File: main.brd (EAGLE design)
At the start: 50.8 x 50.8 mm, 93 parts, among them Q1 5.8A/30V/35mΩ, Q2 5.8A/30V/35mΩ, Q3 2.5A/30V/105mΩ, U1 BQ24133_RGY_24, U2 SN65HVD32_D_8

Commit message: Some layout stuff, package changes
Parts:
- removed 3.3-PWR, ACT, LED: 2V @ 20mA, adafruit:CHIPLED_0603
- removed JP1: (no value), pinhead:1X05
- removed R29, R30: 65, resistor:R0603
- added GPIO: (no value), pinhead:1X10
- added LED0, LED1: 2V @ 20mA, adafruit:CHIPLED_0603
- added R28: 64.9, resistor:R0603
- C10, C11, C12, C14, C15, C18, C19, C20, C21, C25: device rcl:C1206 -> resistor:C0603
- R14, R15, R16, R17, R18: value 1.32k -> ?
- R19, R20, R21, R24, R25: value 680 -> ?
- R41, R42: value 65 -> 64.9
- moved GND-JMP 127.8 mm to (46.5, -28.4)
- moved C23 79.0 mm to (43.1, 16.9), turned to 0 degrees
- moved SD 78.1 mm to (40.8, 26.6), turned to 270 degrees
- moved R31 75.6 mm to (37.0, 17.3), turned to 180 degrees
- moved C9 50.4 mm to (37.8, 35.8)
- moved C1 49.1 mm to (25.1, 33.0), turned to 0 degrees
- moved R27 47.0 mm to (-2.62, -16.5), turned to 270 degrees
- moved AIN 46.1 mm to (2.44, 31.9), turned to 90 degrees
- moved C2 46.1 mm to (25.1, 35.2), turned to 0 degrees
- moved R8 45.9 mm to (-1.91, -21.7), turned to 270 degrees
- moved S2 45.8 mm to (56.9, -17.7), turned to 90 degrees
- moved BATT 45.2 mm to (-0.89, -12.0), turned to 90 degrees
- moved R5 45.2 mm to (23.9, 40.0)
- moved L2 44.7 mm to (-1.55, -19.1), turned to 180 degrees
- moved L6 43.1 mm to (17.3, 43.7), turned to 0 degrees
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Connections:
- removed net LED: MCU.28, R41.1
- removed net N$29: LED.A, R41.2
- removed net VOS: C6.1, L1.2, R3.2, TPS62162-Q1.6
- new net GPIO10: GPIO.10
- new net GPIO6: GPIO.6
- new net GPIO7: GPIO.7
- new net GPIO8: GPIO.8
- new net GPIO9: GPIO.9
- new net N$7: LED0.C, R41.2
- net 3.3V: now also C6.1, L1.2, LED0.A, LED1.A, R3.2, TPS62162-Q1.6; no longer R29.1
- net GND: no longer 3.3-PWR.C, LED.C
- net GPIO1: now also GPIO.1; no longer JP1.1
- net GPIO2: now also GPIO.2; no longer JP1.2
- net GPIO3: now also GPIO.3; no longer JP1.3
- net GPIO4: now also GPIO.4; no longer JP1.4
- net GPIO5: now also GPIO.5; no longer JP1.5
- net N$19: now also SD.2; no longer 3.3-PWR.A, R29.2
- net N$20: now also LED1.C, R28.2; no longer ACT.A, R30.1
- net PB09D_SER4_P1: no longer R30.2
- net SD_CS: no longer ACT.C, SD.2
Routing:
- net AGND: track 37.1 -> 40.2 mm
- net BATT: track 28.2 -> 30.6 mm
- net PC_ACN: track 11.7 -> 12.4 mm
- net PC_VREF: track 16.8 -> 16.2 mm
- net PC_TTC: track 5.02 -> 5.57 mm
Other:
- outline, holes or cut-outs redrawn

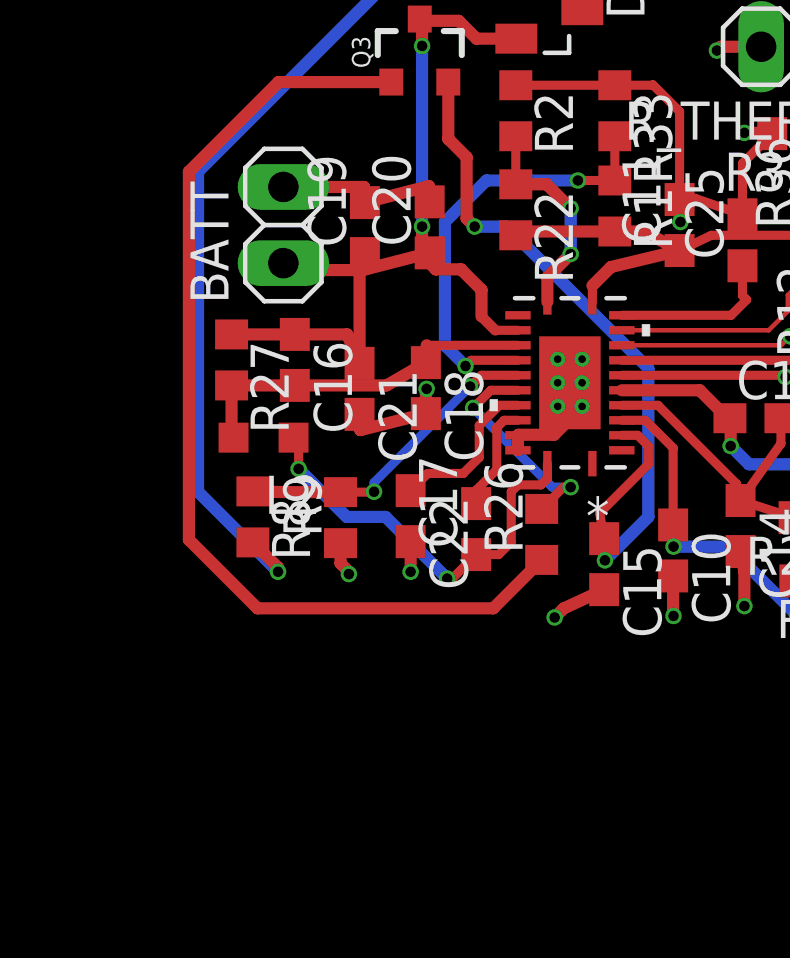
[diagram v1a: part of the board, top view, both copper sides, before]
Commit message: Seperated grounds, added pullup to cell pin
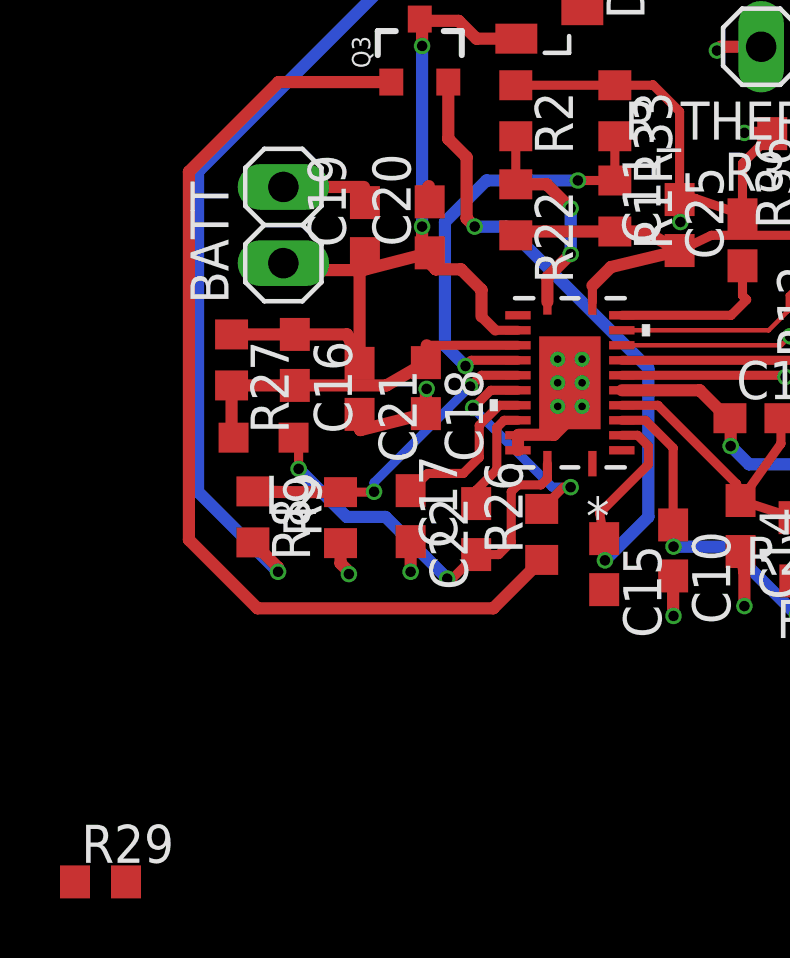
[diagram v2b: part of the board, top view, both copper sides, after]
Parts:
- added R29: 1k, resistor:R0603
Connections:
- net AGND: no longer BATT.2, C12.2, C15.2, C19.2, C20.2, C22.2, U1.22, U1.23
- net GND: now also BATT.2, C12.2, C15.2, C19.2, C20.2, C22.2, U1.22, U1.23
- net PC_CELL: now also R29.2
- net PC_VREF: now also R29.1
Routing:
- net AGND: track 40.2 -> 28.4 mm, vias 10 -> 7
- net GND: track 0.00 -> 7.18 mm, vias 0 -> 2

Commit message: Set adc voltage divider values
Used 100ohm output impedance of ducers and 3.5kohm limit in samd21 datasheet to arrive at the vdiv resistor values.
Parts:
- R14, R15, R16, R17, R18: value ? -> 3.3k
- R19, R20, R21, R24, R25: value ? -> 1.6k
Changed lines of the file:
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@@
 </element>
 <element name="SWD" library="SparkFun-Connectors" package="2X5-PTH-1.27MM" value="CORTEX_DEBUG_PTH" x="28.6258" y="39.7764" rot="R180"/>
-<element name="R14" library="resistor" library_urn="urn:adsk.eagle:library:348" package="R0603" package3d_urn="urn:adsk.eagle:package:26057/1" value="?" x="8.89" y="26.8478"/>
-<element name="R15" library="resistor" library_urn="urn:adsk.eagle:library:348" package="R0603" package3d_urn="urn:adsk.eagle:package:26057/1" value="?" x="8.89" y="29.337"/>
-<element name="R16" library="resistor" library_urn="urn:adsk.eagle:library:348" package="R0603" package3d_urn="urn:adsk.eagle:package:26057/1" value="?" x="8.89" y="31.877"/>
-<element name="R17" library="resistor" library_urn="urn:adsk.eagle:library:348" package="R0603" package3d_urn="urn:adsk.eagle:package:26057/1" value="?" x="8.9154" y="34.4424"/>
-<element name="R18" library="resistor" library_urn="urn:adsk.eagle:library:348" package="R0603" package3d_urn="urn:adsk.eagle:package:26057/1" value="?" x="8.9154" y="36.957"/>
-<element name="R19" library="resistor" library_urn="urn:adsk.eagle:library:348" package="R0603" package3d_urn="urn:adsk.eagle:package:26057/1" value="?" x="5.8674" y="26.8224"/>
-<element name="R20" library="resistor" library_urn="urn:adsk.eagle:library:348" package="R0603" package3d_urn="urn:adsk.eagle:package:26057/1" value="?" x="5.842" y="29.337"/>
-<element name="R21" library="resistor" library_urn="urn:adsk.eagle:library:348" package="R0603" package3d_urn="urn:adsk.eagle:package:26057/1" value="?" x="5.842" y="31.9024"/>
-<element name="R24" library="resistor" library_urn="urn:adsk.eagle:library:348" package="R0603" package3d_urn="urn:adsk.eagle:package:26057/1" value="?" x="5.8674" y="34.4424"/>
-<element name="R25" library="resistor" library_urn="urn:adsk.eagle:library:348" package="R0603" package3d_urn="urn:adsk.eagle:package:26057/1" value="?" x="5.8674" y="36.957"/>
+<element name="R14" library="resistor" library_urn="urn:adsk.eagle:library:348" package="R0603" package3d_urn="urn:adsk.eagle:package:26057/1" value="3.3k" x="8.89" y="26.8478"/>
+<element name="R15" library="resistor" library_urn="urn:adsk.eagle:library:348" package="R0603" package3d_urn="urn:adsk.eagle:package:26057/1" value="3.3k" x="8.89" y="29.337"/>
+<element name="R16" library="resistor" library_urn="urn:adsk.eagle:library:348" package="R0603" package3d_urn="urn:adsk.eagle:package:26057/1" value="3.3k" x="8.89" y="31.877"/>
+<element name="R17" library="resistor" library_urn="urn:adsk.eagle:library:348" package="R0603" package3d_urn="urn:adsk.eagle:package:26057/1" value="3.3k" x="8.9154" y="34.4424"/>
+<element name="R18" library="resistor" library_urn="urn:adsk.eagle:library:348" package="R0603" package3d_urn="urn:adsk.eagle:package:26057/1" value="3.3k" x="8.9154" y="36.957"/>
+<element name="R19" library="resistor" library_urn="urn:adsk.eagle:library:348" package="R0603" package3d_urn="urn:adsk.eagle:package:26057/1" value="1.6k" x="5.8674" y="26.8224"/>
+<element name="R20" library="resistor" library_urn="urn:adsk.eagle:library:348" package="R0603" package3d_urn="urn:adsk.eagle:package:26057/1" value="1.6k" x="5.842" y="29.337"/>
+<element name="R21" library="resistor" library_urn="urn:adsk.eagle:library:348" package="R0603" package3d_urn="urn:adsk.eagle:package:26057/1" value="1.6k" x="5.842" y="31.9024"/>
+<element name="R24" library="resistor" library_urn="urn:adsk.eagle:library:348" package="R0603" package3d_urn="urn:adsk.eagle:package:26057/1" value="1.6k" x="5.8674" y="34.4424"/>
+<element name="R25" library="resistor" library_urn="urn:adsk.eagle:library:348" package="R0603" package3d_urn="urn:adsk.eagle:package:26057/1" value="1.6k" x="5.8674" y="36.957"/>
 <element name="IMU" library="BNO055" package="LGA28R50P4X10_380X520X100" value="BNO055" x="25.4" y="25.4" locked="yes" rot="R180">
 <attribute name="AVAILABILITY" value="Good" x="25.4" y="25.4" size="1.778" layer="27" rot="R180" display="off"/>

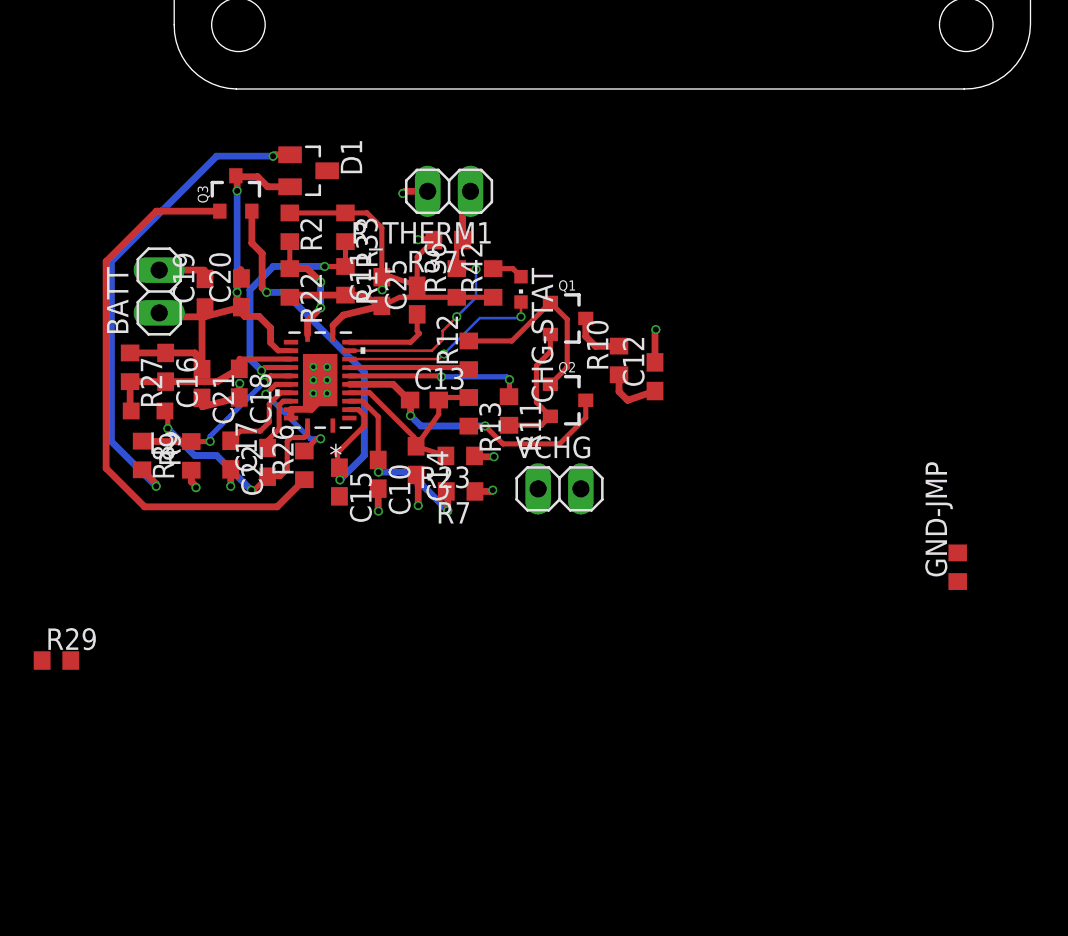
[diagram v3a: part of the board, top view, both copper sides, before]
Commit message: Routing
Need to choose L and sizes for caps and res
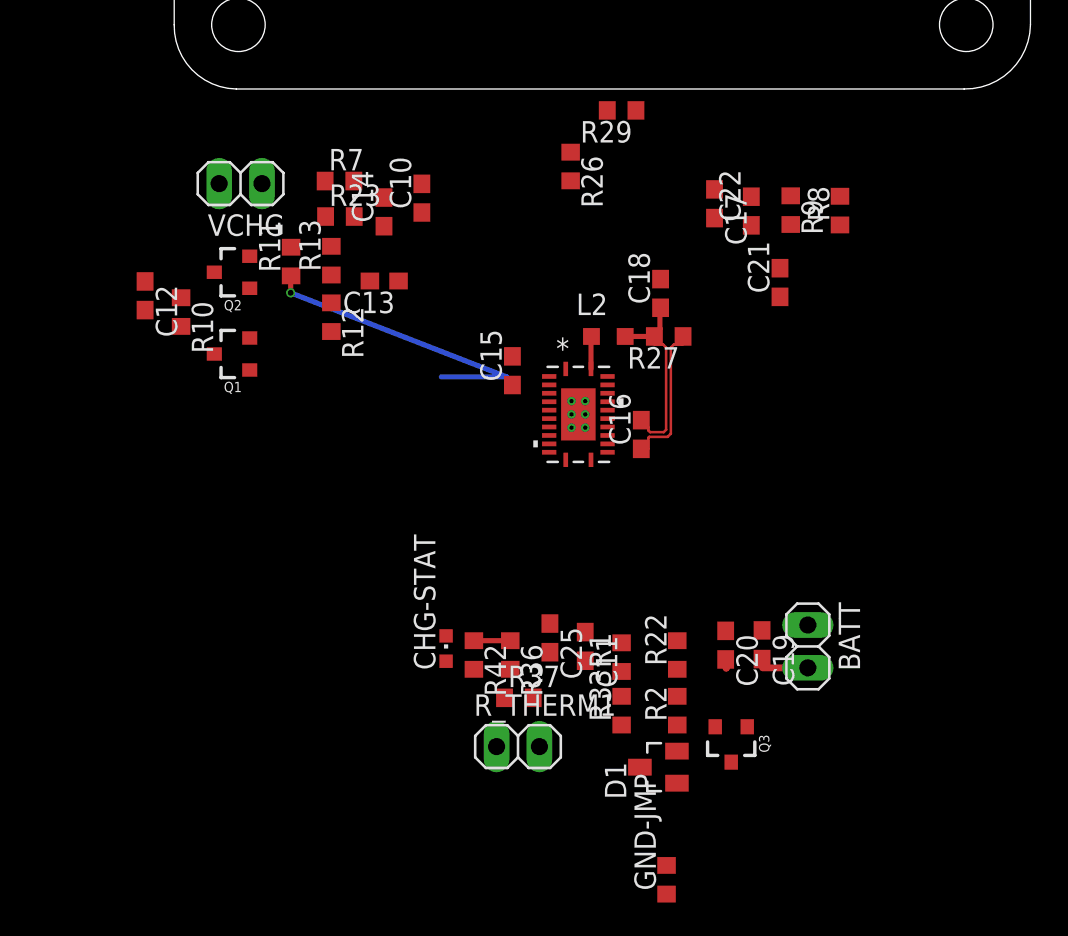
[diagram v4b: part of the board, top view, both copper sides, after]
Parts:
- moved R29 46.8 mm to (26.5, -1.27), turned to 180 degrees
- moved Q3 43.9 mm to (33.0, -38.8), turned to 180 degrees
- moved R8 43.9 mm to (39.5, -7.21), turned to 90 degrees
- moved BATT 43.9 mm to (37.6, -33.1), turned to 270 degrees
- moved D1 41.0 mm to (28.7, -40.2), turned to 90 degrees
- moved C19 39.1 mm to (34.9, -33.0), turned to 270 degrees
- moved R9 38.4 mm to (36.6, -7.19), turned to 270 degrees
- moved R2 36.8 mm to (29.8, -36.9), turned to 90 degrees
- moved C20 35.5 mm to (32.7, -33.0), turned to 270 degrees
- moved C21 34.8 mm to (35.9, -11.5), turned to 90 degrees
- moved C22 34.1 mm to (34.2, -7.24), turned to 90 degrees
- moved R_THERM1 33.2 mm to (20.4, -39.0), turned to 0 degrees
- moved R33 33.0 mm to (26.5, -36.9), turned to 90 degrees
- moved R27 32.0 mm to (29.3, -14.7), turned to 180 degrees
- moved R22 31.9 mm to (29.8, -33.6), turned to 90 degrees
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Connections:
- net PC_AVCC renamed N$21
- net PC_NBATDRV renamed *BATDRV
- net PC_STAT: now also R36.2, R37.1, R_THERM1.1
- net PC_TS: no longer R36.2, R37.1, R_THERM1.1
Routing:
- net N$10: track 33.6 -> 0.00 mm
- net VIN: track 32.3 -> 0.00 mm, vias 2 -> 0
- net AGND: track 28.4 -> 0.04 mm, vias 7 -> 0
- net PC_PVCC: track 26.8 -> 0.00 mm, vias 3 -> 0
- net BATT: track 30.6 -> 8.87 mm, vias 2 -> 0
- net PC_ACP: track 18.7 -> 0.00 mm, vias 2 -> 0
- net PC_TS: track 16.9 -> 0.00 mm, vias 2 -> 0
- net PC_ACSET: track 14.6 -> 0.00 mm, vias 2 -> 0
- net PC_VREF: track 16.2 -> 2.16 mm
- net PC_ACN: track 12.4 -> 0.00 mm
- net PC_STAT: track 12.1 -> 0.00 mm, vias 2 -> 0
- net PC_SW: track 13.8 -> 1.94 mm, vias 2 -> 0
- net N$21: track 11.6 -> 0.00 mm, vias 2 -> 0
- net N$17: track 11.5 -> 0.00 mm
- net PC_OVPSET: track 10.6 -> 0.00 mm, vias 2 -> 0
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
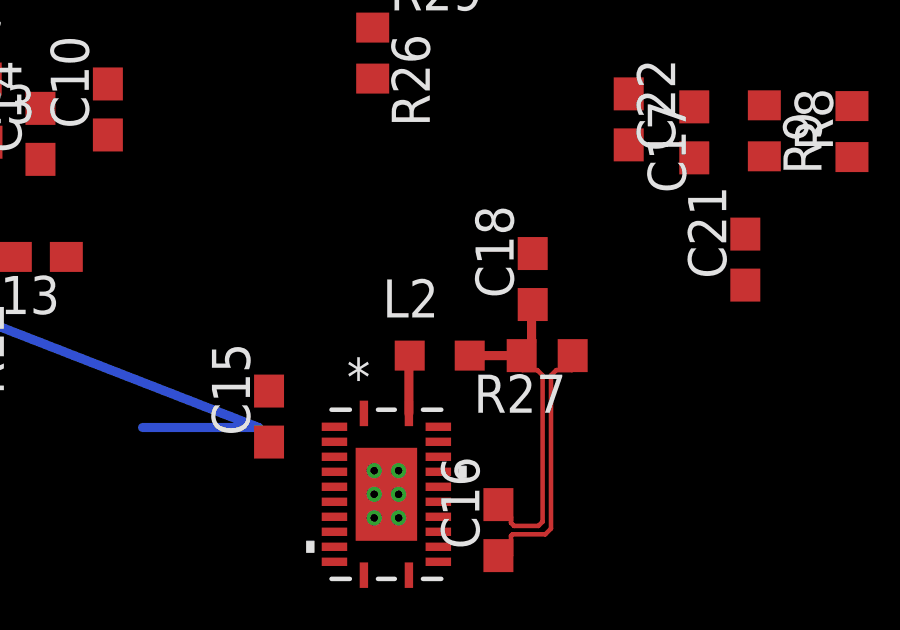
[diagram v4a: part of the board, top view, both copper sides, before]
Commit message: Still need to change pad sizes
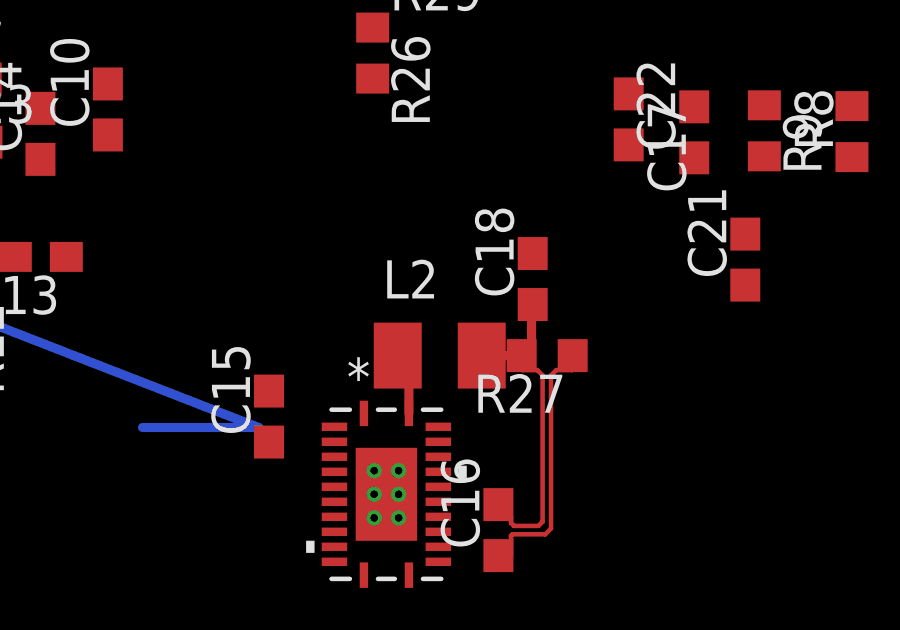
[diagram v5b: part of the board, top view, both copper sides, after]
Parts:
- L2: device resistor:L2012C -> rcl:L3225M
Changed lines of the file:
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@@
 <?xml version="1.0" encoding="utf-8"?>
 <!DOCTYPE eagle SYSTEM "eagle.dtd">
-<eagle version="8.6.0">
+<eagle version="8.5.1">
 <drawing>
 <settings>
@@
 </element>
 <element name="R26" library="resistor" package="R0603" value="1k" x="23.5204" y="-4.5974" rot="R270"/>
-<element name="L2" library="resistor" package="L2012C" value="3.3u" x="25.7556" y="-14.6812"/>
+<element name="L2" library="rcl" library_urn="urn:adsk.eagle:library:334" package="L3225M" package3d_urn="urn:adsk.eagle:package:23477/1" value="3.3u" x="25.7556" y="-14.6812">
+<attribute name="SPICEPREFIX" value="L" x="25.7556" y="-14.6812" size="1.778" layer="27" display="off"/>
+</element>
 <element name="R27" library="resistor" package="R0603" value="10m" x="29.337" y="-14.6812" rot="R180"/>
 <element name="C16" library="resistor" package="C0603" value="100n" x="27.7114" y="-20.4978" rot="R90"/>
@@
 <wire x1="29.0449" y1="-20.3581" x2="29.1846" y2="-20.2184" width="0.1524" layer="1"/>
 <wire x1="28.2321" y1="-20.3581" x2="29.0449" y2="-20.3581" width="0.1524" layer="1"/>
-<wire x1="26.7556" y1="-14.6812" x2="28.487" y2="-14.6812" width="0.3048" layer="1"/>
+<wire x1="27.1556" y1="-14.6812" x2="28.487" y2="-14.6812" width="0.3048" layer="1"/>
 <wire x1="28.487" y1="-14.6812" x2="28.487" y2="-14.5787" width="0.3048" layer="1"/>
 <wire x1="28.487" y1="-14.5787" x2="28.8163" y2="-14.2494" width="0.3048" layer="1"/>
@@
 <contactref element="U1" pad="24"/>
 <wire x1="24.7276" y1="-16.608" x2="24.7276" y2="-14.7092" width="0.3048" layer="1"/>
-<wire x1="24.7276" y1="-14.7092" x2="24.7556" y2="-14.6812" width="0.3048" layer="1"/>
-<wire x1="24.7556" y1="-14.6812" x2="32.0548" y2="-5.9572" width="0" layer="19" extent="1-1"/>
+<wire x1="24.7276" y1="-14.7092" x2="24.3556" y2="-14.6812" width="0.3048" layer="1"/>
+<wire x1="24.3556" y1="-14.6812" x2="32.0548" y2="-5.9572" width="0" layer="19" extent="1-1"/>
 </signal>
 <signal name="PC_ACSET">
@@
 </board>
 </drawing>
+<compatibility>
+<note version="8.2" severity="warning">
+Since Version 8.2, EAGLE supports online libraries. The ids
+of those online libraries will not be understood (or retained)
+with this version.
+</note>
+<note version="8.3" severity="warning">
+Since Version 8.3, EAGLE supports URNs for individual library
+assets (packages, symbols, and devices). The URNs of those assets
+will not be understood (or retained) with this version.
+</note>
+<note version="8.3" severity="warning">
+Since Version 8.3, EAGLE supports the association of 3D packages
+with devices in libraries, schematics, and board files. Those 3D
+packages will not be understood (or retained) with this version.
+</note>
+</compatibility>
 </eagle>

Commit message: More value changes, package updates needed
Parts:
- removed C20: 10u, resistor:C0603
- 103AT-THERMISTOR: value 103AT -> 10k
- C1, C2: value 0.1uF -> 100n
- C23, C3, C5, C8, C9: value 100nF -> 100n
- C4: value 6.8nF -> 6.8n
- C7: device rcl:C1206 -> resistor:C0603
- L2: value 3.3u -> 6.8u; device rcl:L3225M -> ipc-7351-inductor:INDC2520X220N
- R2: value 36.6k -> 3.8k
- R22: value 232k -> 100k
- R33: value 153.9k -> 13.8k
- R9: value 100k -> 113k
- moved C7 88.2 mm to (-2.51, -50.9), turned to 0 degrees
- renumbered R_THERM1 to 103AT-THERMISTOR
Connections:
- removed net PC_PVCC_2: U1.2
- removed net PC_SW_2: U1.1
- net BATT: no longer C20.1
- net GND: no longer C20.2
- net PC_PVCC: now also U1.2
- net PC_STAT: no longer 103AT-THERMISTOR.1, R36.2, R37.1
- net PC_SW: now also U1.1
- net PC_TS: now also 103AT-THERMISTOR.1, R36.2, R37.1
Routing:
- net GND: track 3.71 -> 2.69 mm

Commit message: layout overlook
Done
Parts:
- moved R5 7.72 mm to (24.3, 32.3), turned to 180 degrees
- moved C5 6.58 mm to (23.1, 29.3)
- moved C3 3.69 mm to (18.3, 41.2)
- moved C1 3.44 mm to (24.3, 36.4)
- moved C4 2.19 mm to (21.0, 28.5), turned to 90 degrees
- moved C9 1.75 mm to (36.8, 37.2)
- moved L6 1.38 mm to (18.6, 43.0), turned to 180 degrees
- moved C2 1.16 mm to (24.3, 34.3)
- moved C23 0.79 mm to (43.7, 17.3), turned to 180 degrees
- moved C8 0.06 mm to (27.3, 29.4)
